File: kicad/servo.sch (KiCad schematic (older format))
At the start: 0 parts

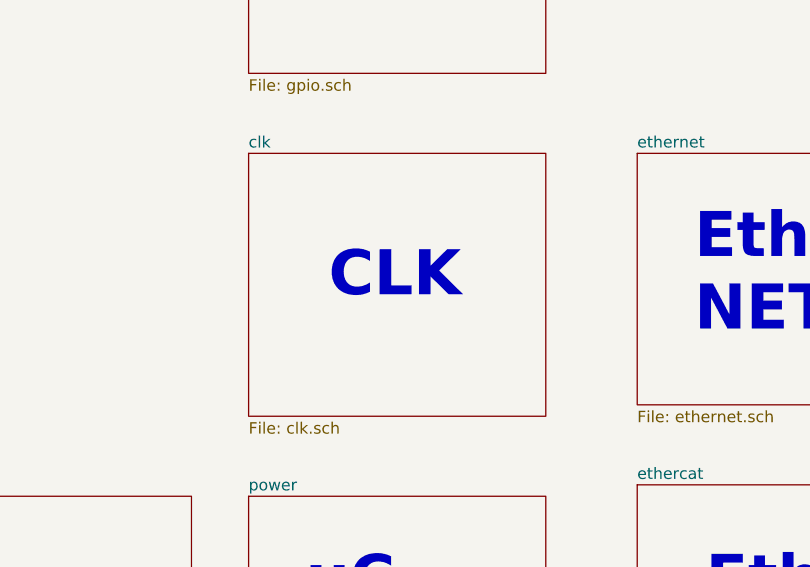
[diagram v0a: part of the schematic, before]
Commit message: I've connected interfaces to gpio and change some muxes
I've changed some muxes reading the datasheet to group same kind of
signals, now it's time to add encoders input
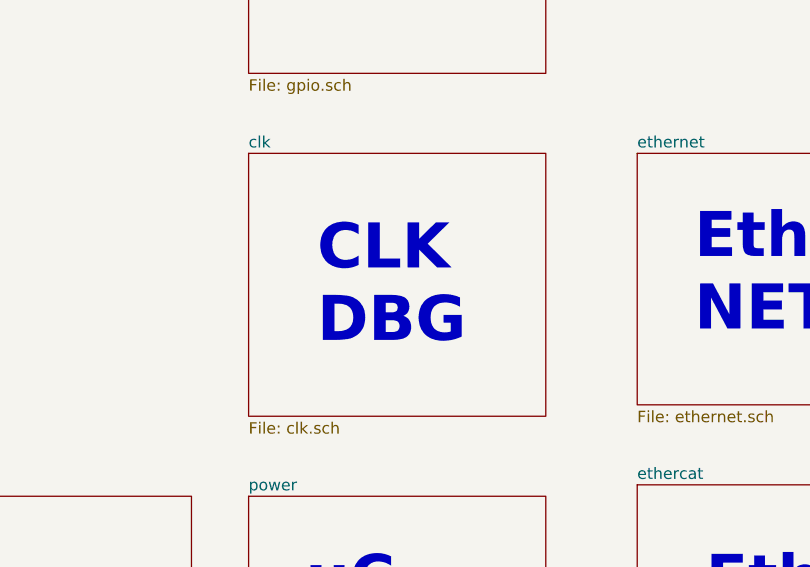
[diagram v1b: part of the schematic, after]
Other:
- note added: "CLK\nDBG"
- note removed: "CLK"
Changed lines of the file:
@@
 Text Notes 6450 3400 0    197  ~ 39
 Ether\nNET
-Text Notes 4850 3250 0    197  ~ 39
-CLK
+Text Notes 4800 3450 0    197  ~ 39
+CLK\nDBG
 $EndSCHEMATC

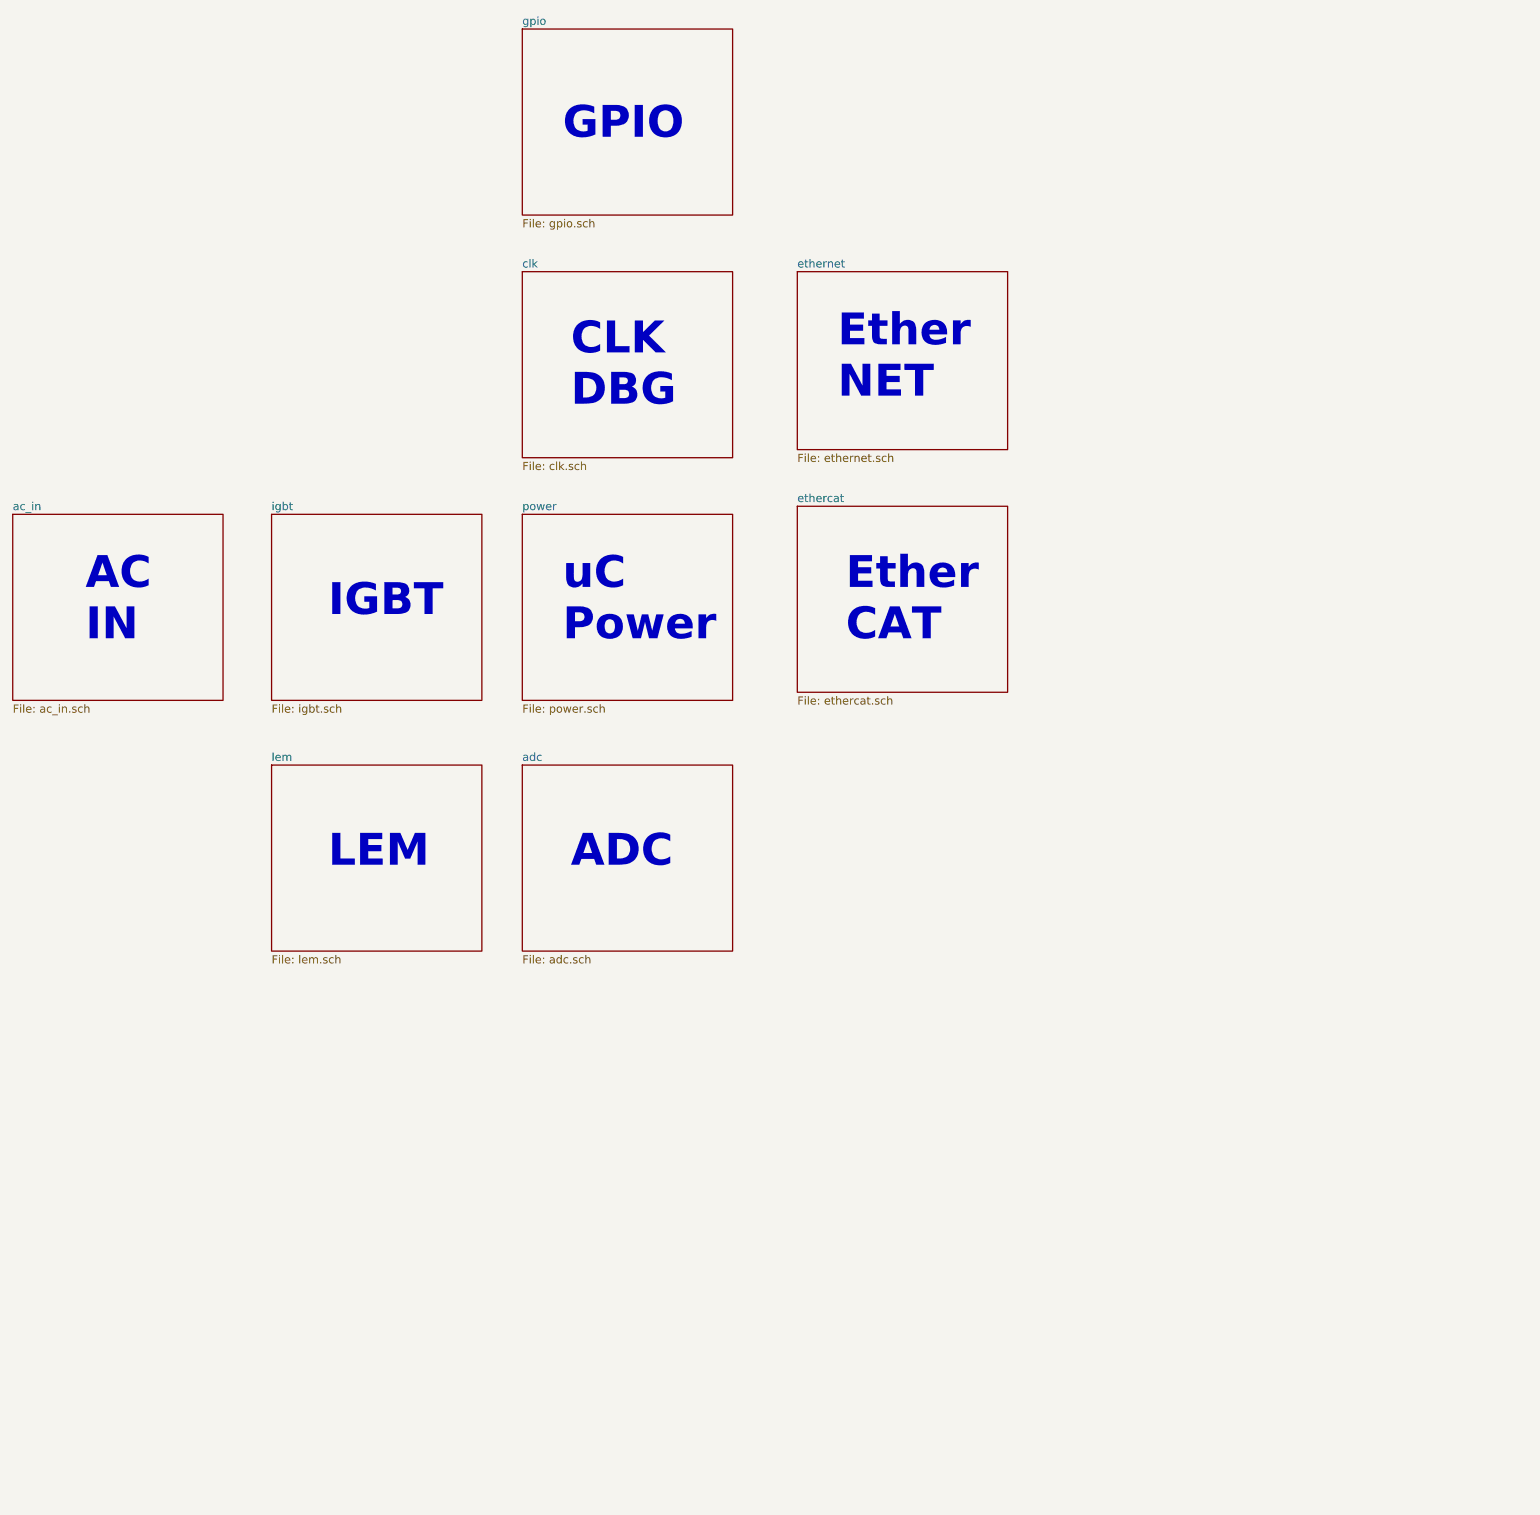
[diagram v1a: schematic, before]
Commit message: added can, rs485, qep endat and others details
I've added a lot of interfases and route his pins to gpios... keep going
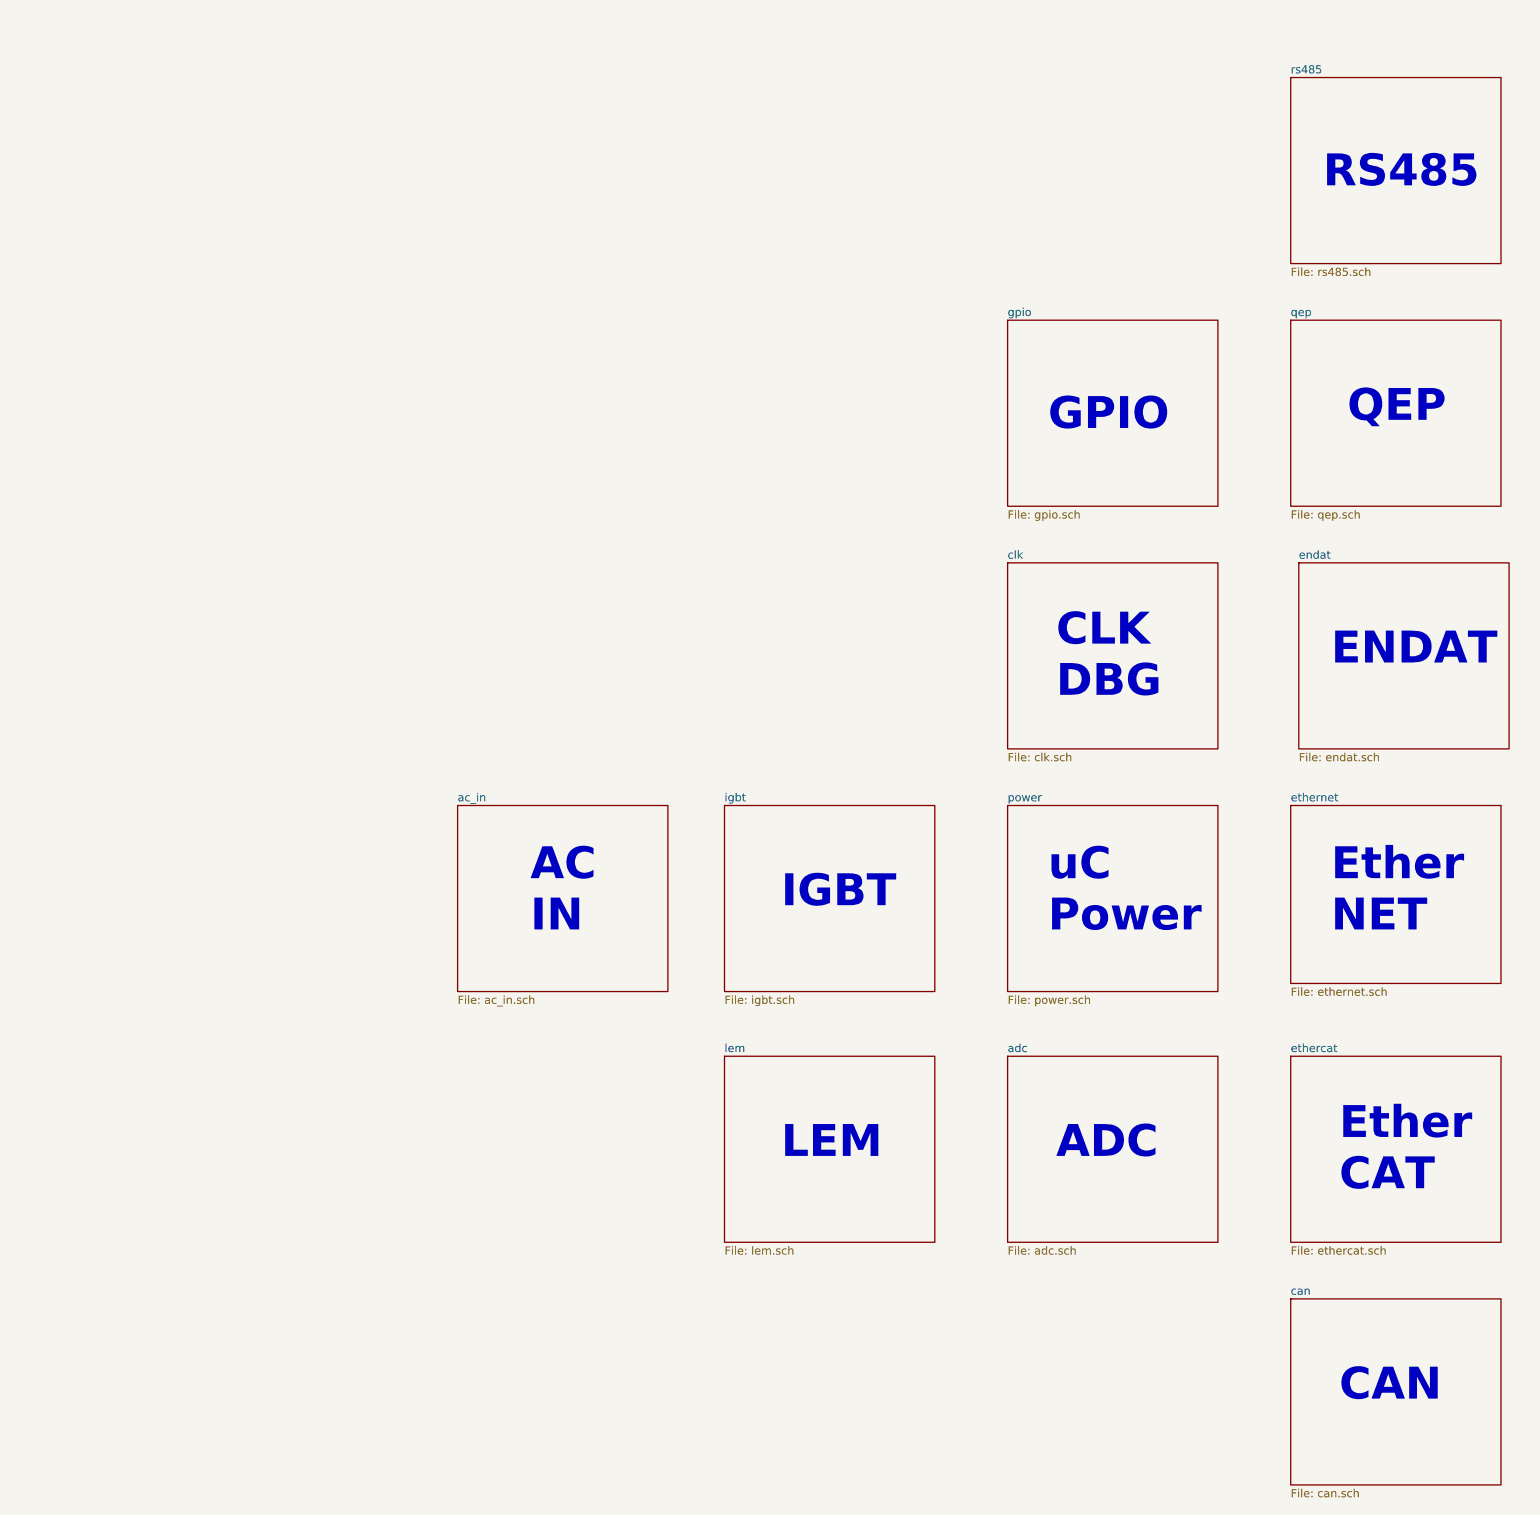
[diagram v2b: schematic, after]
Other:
- note added: "CAN"
- note added: "ENDAT"
- note added: "QEP"
- note added: "RS485"
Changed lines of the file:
@@
 EELAYER 26 0
 EELAYER END
-$Descr A4 11693 8268
+$Descr A3 16535 11693
 encoding utf-8
-Sheet 1 10
+Sheet 1 14
 Title "servo drive"
 Date "25 10 2019"
@@
 $EndDescr
 $Sheet
-S 6200 2600 1300 1100
+S 9250 5900 1300 1100
 U 5DC3DC9E
 F0 "ethernet" 50
@@
 $EndSheet
 $Sheet
-S 4500 5650 1300 1150
+S 7500 7450 1300 1150
 U 5DD0E9D6
 F0 "adc" 50
@@
 $EndSheet
 $Sheet
-S 6200 4050 1300 1150
+S 9250 7450 1300 1150
 U 5DC4A59D
 F0 "ethercat" 50
@@
 $EndSheet
 $Sheet
-S 4500 4100 1300 1150
+S 7500 5900 1300 1150
 U 5EAA846A
 F0 "power" 50
@@
 $EndSheet
 $Sheet
-S 4500 2600 1300 1150
+S 7500 4400 1300 1150
 U 5DD4DF4C
 F0 "clk" 50
@@
 $EndSheet
 $Sheet
-S 1350 4100 1300 1150
+S 4100 5900 1300 1150
 U 5DD76B18
 F0 "ac_in" 50
@@
 $EndSheet
 $Sheet
-S 2950 5650 1300 1150
+S 5750 7450 1300 1150
 U 5DF5EE96
 F0 "lem" 50
 F1 "lem.sch" 50
 $EndSheet
-Text Notes 3300 6300 0    197  ~ 39
+Text Notes 6100 8100 0    197  ~ 39
 LEM
-Text Notes 4800 6300 0    197  ~ 39
+Text Notes 7800 8100 0    197  ~ 39
 ADC
 $Sheet
-S 2950 4100 1300 1150
+S 5750 5900 1300 1150
 U 5DDE8C5E
 F0 "igbt" 50
 F1 "igbt.sch" 50
 $EndSheet
-Text Notes 3300 4750 0    197  ~ 39
+Text Notes 6100 6550 0    197  ~ 39
 IGBT
-Text Notes 4750 4900 0    197  ~ 39
+Text Notes 7750 6700 0    197  ~ 39
 uC \nPower
-Text Notes 6500 4900 0    197  ~ 39
+Text Notes 9550 8300 0    197  ~ 39
 Ether\nCAT
 $Sheet
-S 4500 1100 1300 1150
+S 7500 2900 1300 1150
 U 5DE49152
 F0 "gpio" 50
 F1 "gpio.sch" 50
 $EndSheet
-Text Notes 4750 1800 0    197  ~ 39
+Text Notes 7750 3600 0    197  ~ 39
 GPIO
-Text Notes 1800 4900 0    197  ~ 39
+Text Notes 4550 6700 0    197  ~ 39
 AC\nIN
-Text Notes 6450 3400 0    197  ~ 39
+Text Notes 9500 6700 0    197  ~ 39
 Ether\nNET
-Text Notes 4800 3450 0    197  ~ 39
+Text Notes 7800 5250 0    197  ~ 39
 CLK\nDBG
+Text Notes 9500 5050 0    197  ~ 39
+ENDAT
+$Sheet
+S 9300 4400 1300 1150
+U 5DE3DF56
+F0 "endat" 50
+F1 "endat.sch" 50
+$EndSheet
+$Sheet
+S 9250 2900 1300 1150
+U 5E092156
+F0 "qep" 50
+F1 "qep.sch" 50
+$EndSheet
+Text Notes 9600 3550 0    197  ~ 39
+QEP
+$Sheet
+S 9250 1400 1300 1150
+U 5E1BAEAA
+F0 "rs485" 50
+F1 "rs485.sch" 50
+$EndSheet
+Text Notes 9450 2100 0    197  ~ 39
+RS485
+$Sheet
+S 9250 8950 1300 1150
+U 5E21534F
+F0 "can" 50
+F1 "can.sch" 50
+$EndSheet
+Text Notes 9550 9600 0    197  ~ 39
+CAN
 $EndSCHEMATC

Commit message: added shunt using sigma delta, just fot 1 channel
I've added a sigma delta isolated sampler for use with shunt in phase
measurement. 'cose it seems is the best accuracy method for current
measurement, but it implies a lot of componentes, 8 PWM lines to
generate the sigma delta clk, or maybe I'd use only one clk for all
sigma deltas, ..I've to think about it, but it seems that should be
better than Hall.. working on that
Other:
- note added: "SHUNT"
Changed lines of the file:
@@
 $Descr A3 16535 11693
 encoding utf-8
-Sheet 1 14
+Sheet 1 15
 Title "servo drive"
 Date "25 10 2019"
@@
 Text Notes 9550 9600 0    197  ~ 39
 CAN
+$Sheet
+S 5750 4350 1300 1150
+U 5DEE980E
+F0 "shunt" 50
+F1 "shunt.sch" 50
+$EndSheet
+Text Notes 5900 5100 0    197  ~ 39
+SHUNT
 $EndSCHEMATC

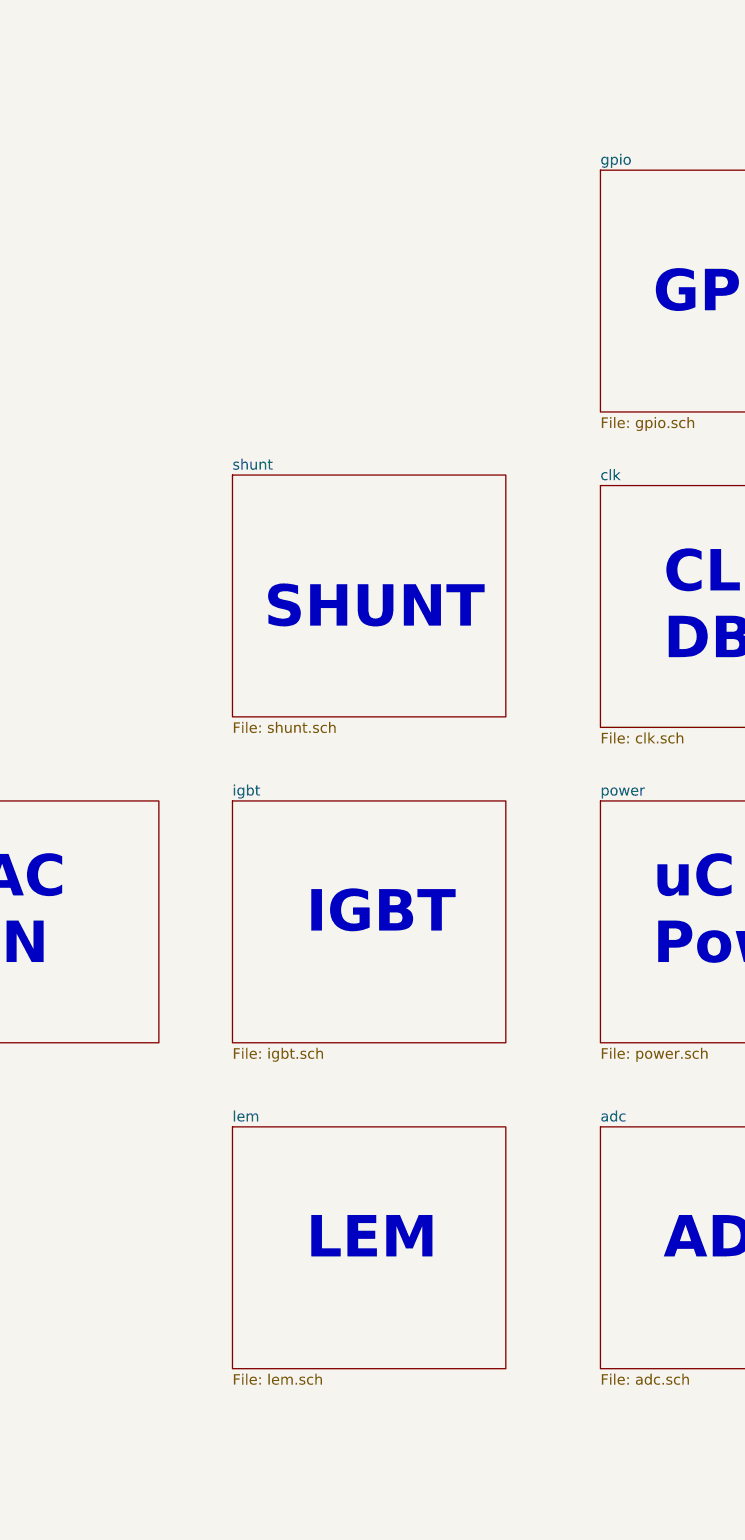
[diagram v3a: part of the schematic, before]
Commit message: Added diff adc isolated to add more adc channels
I've added isolated adc's ACM1100 in adition of ACM1304, 'cose C2000
only has 4 sigmadelta filter, and for 2 motors I need 6 for phase
measurement and 1 for BUS voltage measurement. So I'll have to decide if
I eliminate the hall sensores, becosue, using 7 isolated diff adc plus 4
sigma delta is enough to the requeriments... or instead eliminate all
sigma delta too and left only adc diff isolated.. I think these will be
the best option...
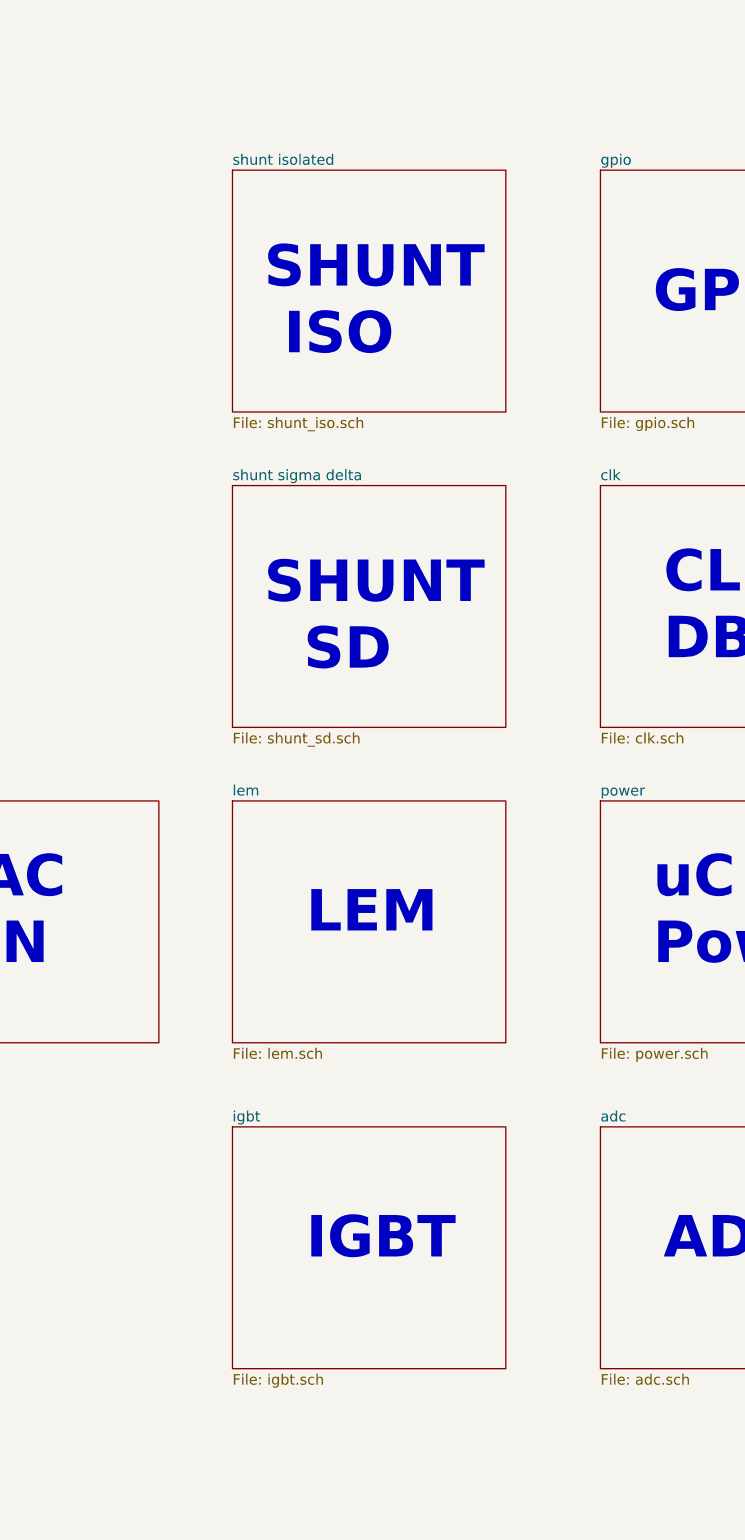
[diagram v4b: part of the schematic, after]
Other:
- note added: "SHUNT\n ISO"
- note added: "SHUNT\n SD"
- note removed: "SHUNT"
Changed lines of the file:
@@
 $Descr A3 16535 11693
 encoding utf-8
-Sheet 1 15
+Sheet 1 16
 Title "servo drive"
 Date "25 10 2019"
@@
 $EndSheet
 $Sheet
-S 5750 7450 1300 1150
+S 5750 5900 1300 1150
 U 5DF5EE96
 F0 "lem" 50
 F1 "lem.sch" 50
 $EndSheet
-Text Notes 6100 8100 0    197  ~ 39
+Text Notes 6100 6550 0    197  ~ 39
 LEM
 Text Notes 7800 8100 0    197  ~ 39
 ADC
 $Sheet
-S 5750 5900 1300 1150
+S 5750 7450 1300 1150
 U 5DDE8C5E
 F0 "igbt" 50
 F1 "igbt.sch" 50
 $EndSheet
-Text Notes 6100 6550 0    197  ~ 39
+Text Notes 6100 8100 0    197  ~ 39
 IGBT
 Text Notes 7750 6700 0    197  ~ 39
@@
 CAN
 $Sheet
-S 5750 4350 1300 1150
+S 5750 4400 1300 1150
 U 5DEE980E
-F0 "shunt" 50
-F1 "shunt.sch" 50
+F0 "shunt sigma delta" 50
+F1 "shunt_sd.sch" 50
 $EndSheet
-Text Notes 5900 5100 0    197  ~ 39
-SHUNT
+Text Notes 5900 5300 0    197  ~ 39
+SHUNT\n  SD
+$Sheet
+S 5750 2900 1300 1150
+U 5E2F3BE3
+F0 "shunt isolated" 50
+F1 "shunt_iso.sch" 50
+$EndSheet
+Text Notes 5900 3800 0    197  ~ 39
+SHUNT\n ISO
 $EndSCHEMATC
